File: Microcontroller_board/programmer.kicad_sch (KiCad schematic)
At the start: 15 parts, among them J1 USB_B_Micro, J2 Conn_01x07_Pin, Q1 BC817, Q2 BC817, U2 CP2102N-Axx-xQFN28

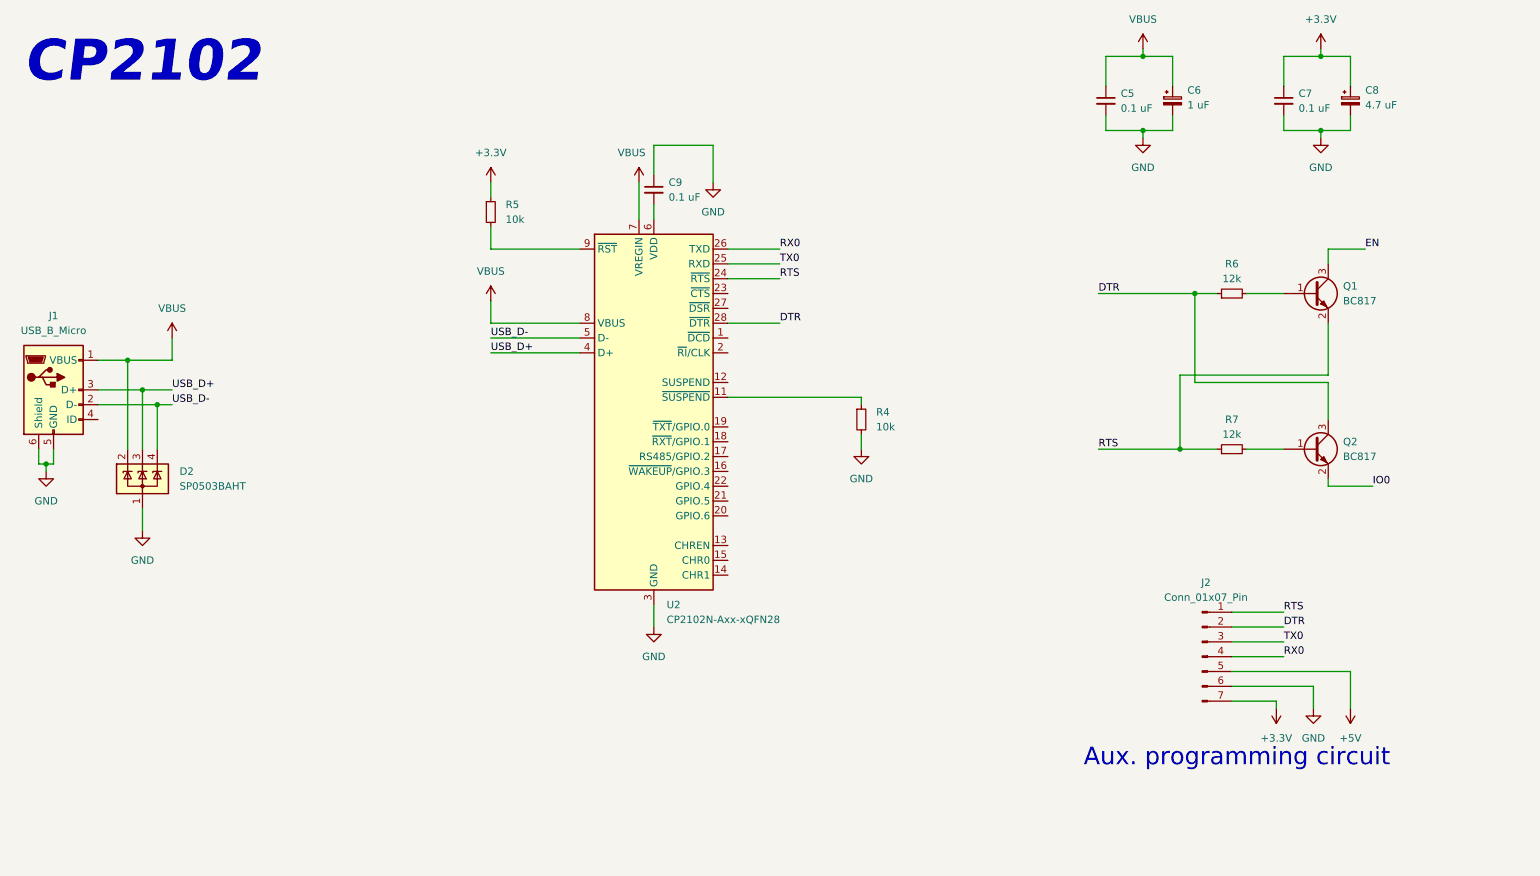
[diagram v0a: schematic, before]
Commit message: Added more pages, CP and RS485
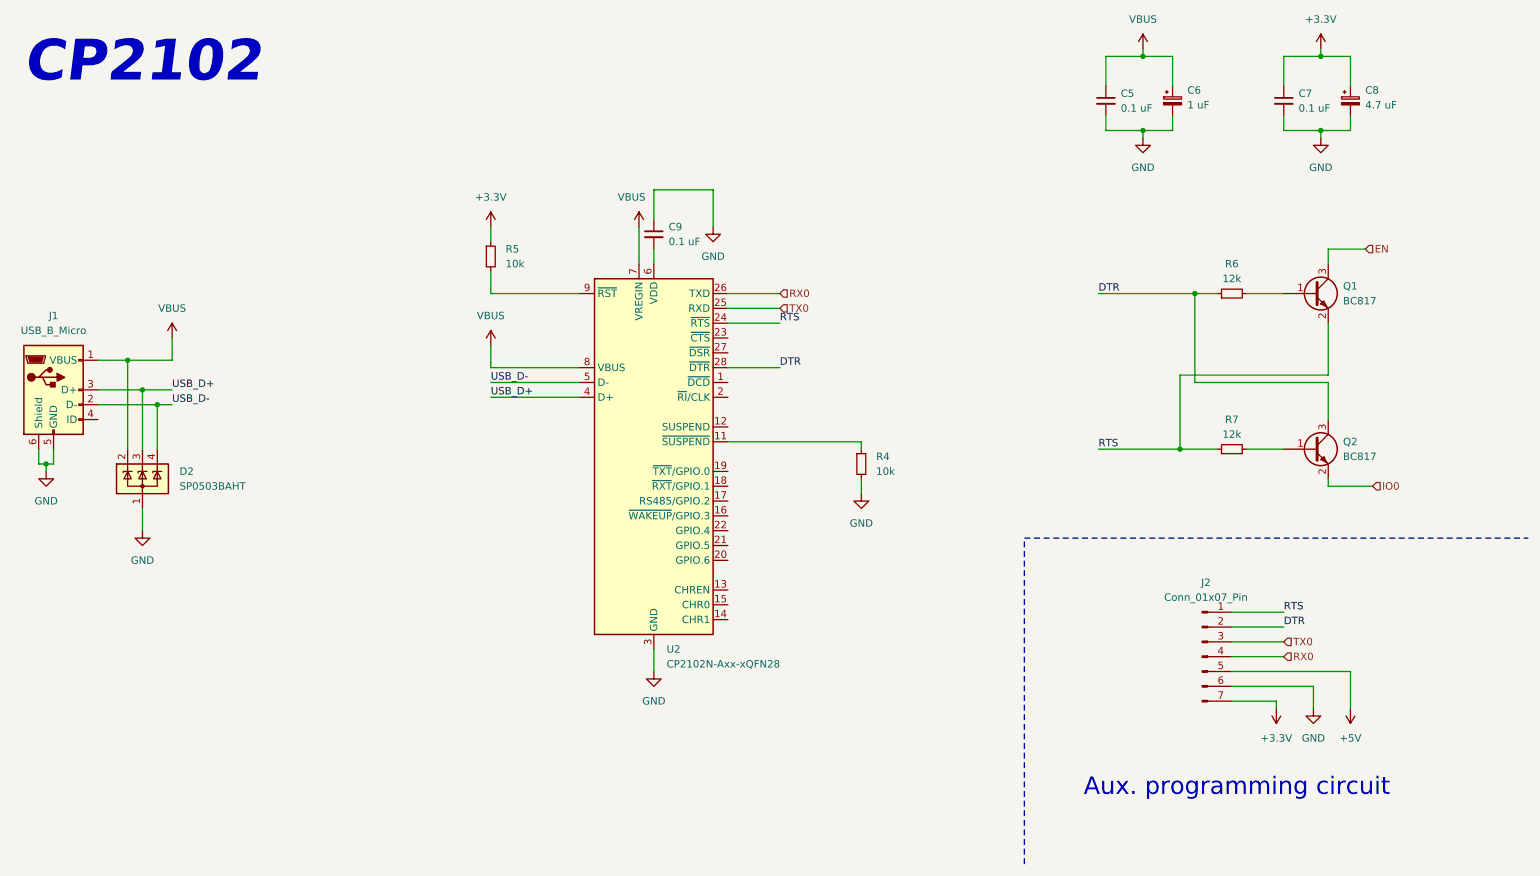
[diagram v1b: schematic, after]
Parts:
- J1: Cód. proveedor (none) -> C8351-05BFDGNBFR; Proveedor (none) -> Elemon
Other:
- moved on the sheet: C9, R4, R5, U2

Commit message: Delete sensingboard project and add stm32 micro to the schematic
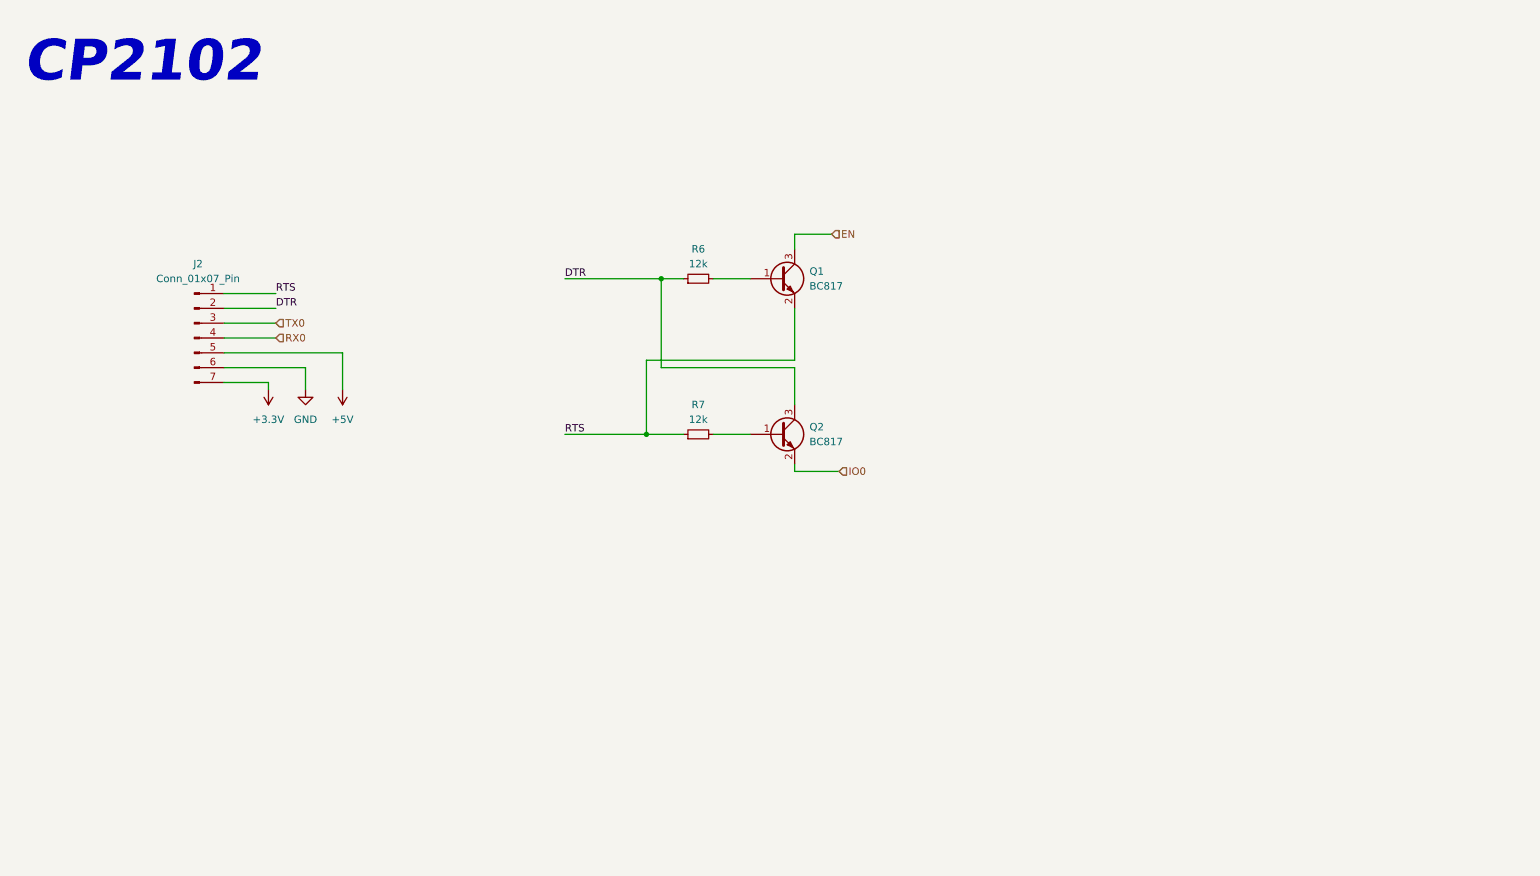
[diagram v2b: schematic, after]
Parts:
- removed C5, C7, C9: 0.1 uF, symbol Device:C_Small
- removed C6: 1 uF, symbol Device:C_Polarized_Small
- removed C8: 4.7 uF, symbol Device:C_Polarized_Small
- removed D2: SP0503BAHT, Package_TO_SOT_SMD:SOT-143, symbol Power_Protection:SP0503BAHT
- removed J1: USB_B_Micro, symbol Connector:USB_B_Micro
- removed R4, R5: 10k, symbol Device:R_Small
- removed U2: CP2102N-Axx-xQFN28, Package_DFN_QFN:QFN-28-1EP_5x5mm_P0.5mm_EP3.35x3.35mm, symbol Interface_USB:CP2102N-Axx-xQFN28
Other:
- note removed: "Aux. programming circuit"
- moved on the sheet: J2, Q1, Q2, R6, R7
